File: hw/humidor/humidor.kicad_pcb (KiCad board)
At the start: 2 copper layers, 79 x 53 mm, 26 parts, among them J1 PWR IN, J2 PWR IN/EXTSENS/IND, J3 IN_SENSOR, J4 Conn_01x05, J5 HEAT/FAN/HS, Q1 2N7002, Q2 IRFD9120, Q3 IRL540, SW1 SW_Push, U1 LT1086-ADJ

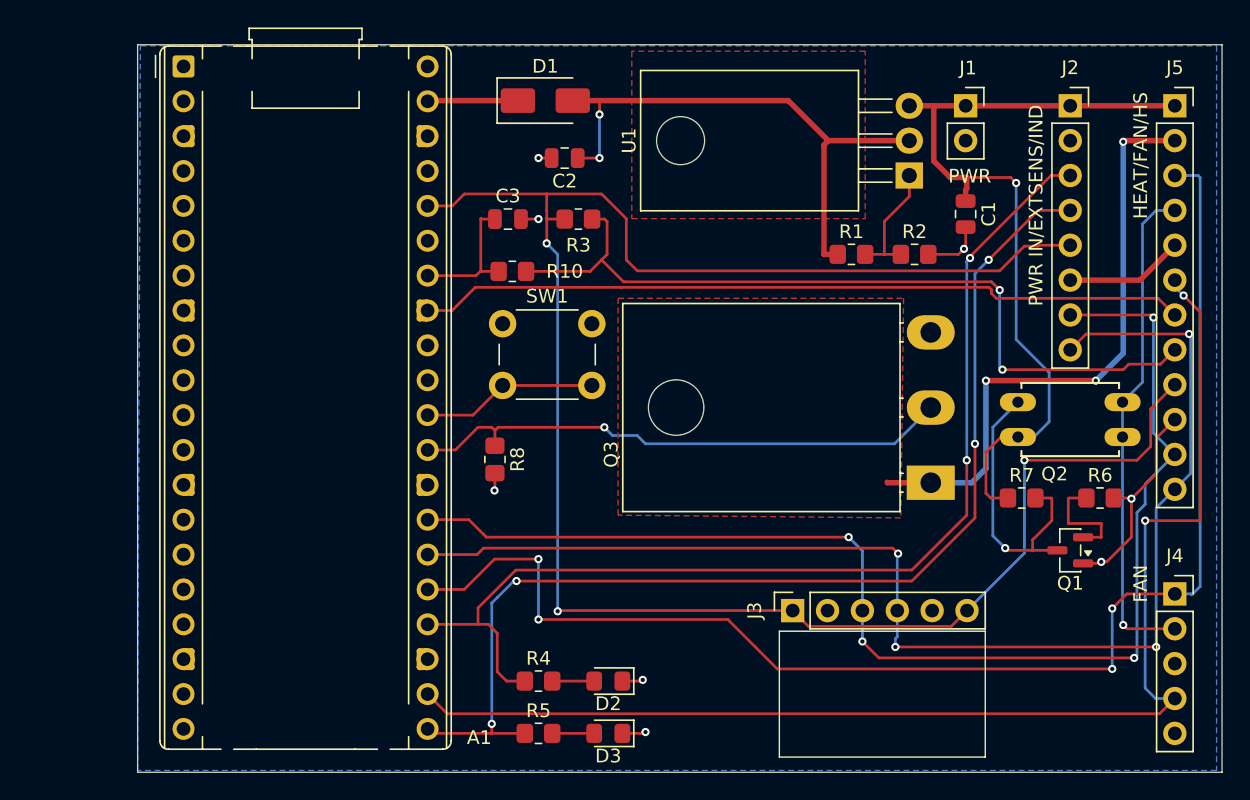
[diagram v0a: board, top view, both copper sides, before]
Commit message: finalized board with all DRC satisfied. Next step is to try double side layout.
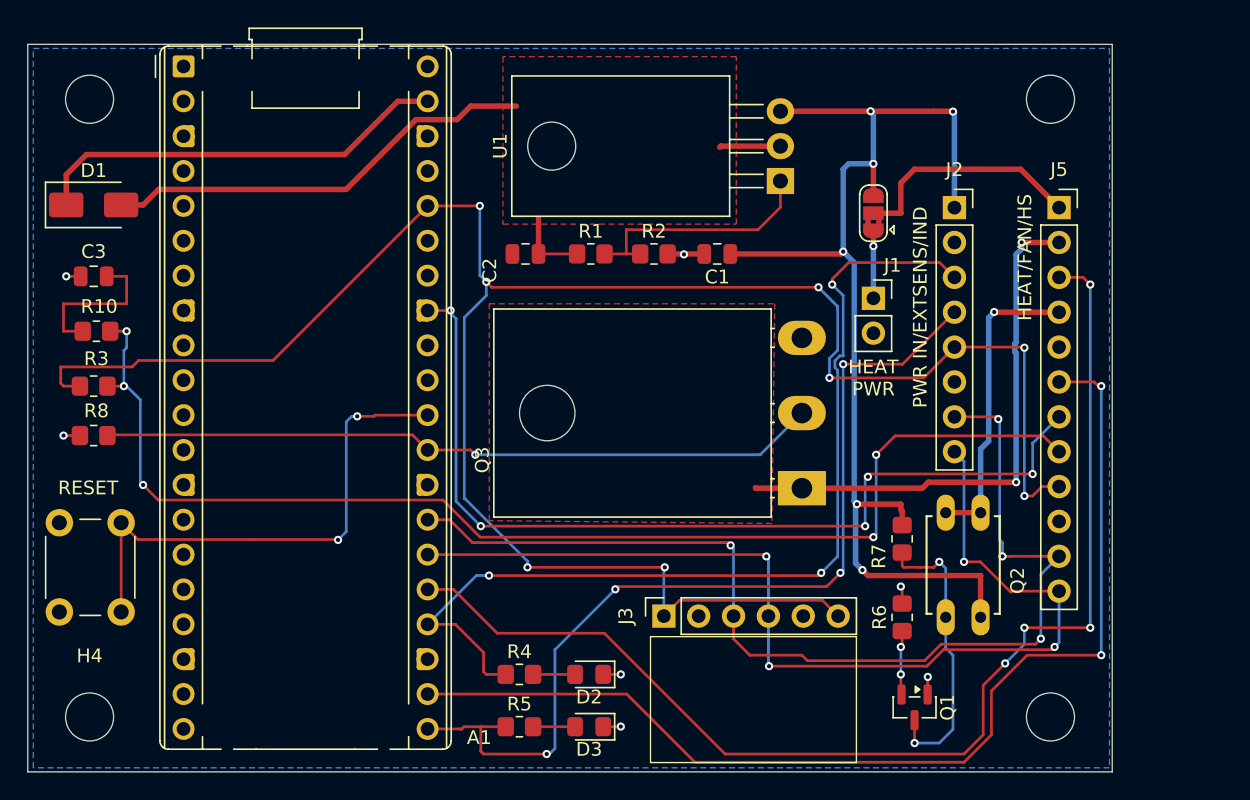
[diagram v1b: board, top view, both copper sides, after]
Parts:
- removed J4: Conn_01x05, Connector_PinSocket_2.54mm:PinSocket_1x05_P2.54mm_Vertical
- added H1: MountingHole, MountingHole:MountingHole_3.5mm, F.Cu at (153.5, 53.5)
- added H2: MountingHole, MountingHole:MountingHole_3.5mm, F.Cu at (153.5, 98.5)
- added H3: MountingHole, MountingHole:MountingHole_3.5mm, F.Cu at (83.5, 53.5)
- added H4: MountingHole, MountingHole:MountingHole_3.5mm, F.Cu at (83.5, 98.5)
- added JP2: SolderJumper_3_Bridged12, Jumper:SolderJumper-3_P1.3mm_Bridged2Bar12_RoundedPad1.0x1.5mm, F.Cu at (140.6, 61.8)
- moved SW1 38.5 mm to (81.3, 90.8), turned to 90 degrees
- moved R3 37.3 mm to (83.8, 74.4)
- moved D1 33.8 mm to (83.8, 61.2)
- moved R10 30.6 mm to (84.0, 70.4)
- moved C3 30.5 mm to (83.8, 66.4), turned to 180 degrees
- moved R8 29.3 mm to (83.8, 78.0), turned to 180 degrees
- moved R1 19.0 mm to (120.0, 64.8)
- moved R2 19.0 mm to (124.6, 64.8)
- moved C1 18.3 mm to (129.2, 64.8), turned to 180 degrees
- moved R6 16.8 mm to (142.7, 91.2), turned to 90 degrees
- moved Q1 16.1 mm to (143.6, 97.8), turned to -90 degrees
- moved J1 15.6 mm to (140.6, 68.0)
- moved Q2 13.2 mm to (147.1, 87.4), turned to -90 degrees
- moved J2 11.2 mm to (146.5, 61.4)
- moved J5 11.2 mm to (154.1, 61.4)
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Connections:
- J1 pad 1: +12V -> Net-(J1-Pin_1)
- J5 pad 1: +12V -> /HEAT_PWR
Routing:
- net /T_HEATSINK: track 58.9 -> 89.6 mm, vias 2 -> 5
- net GND: track 35.3 -> 10.1 mm, vias 8 -> 7
- net Net-(A1-RUN): track 12.9 -> 37.8 mm, vias 0 -> 2
- net Net-(A1-VSYS): track 6.60 -> 30.7 mm
- net +12V: track 60.4 -> 82.9 mm, vias 1 -> 6
- net /SDA0: track 93.5 -> 74.6 mm
- net /HEAT_PWR: track 0.00 -> 17.3 mm
- net /SCL0: track 92.3 -> 77.5 mm
- net /FAN_PWR: track 36.5 -> 22.3 mm
- net /FAN_PWM: track 92.5 -> 79.0 mm
- net /FAN_ON: track 81.1 -> 68.5 mm
- net +3.3V: track 142.4 -> 155.0 mm, vias 3 -> 8
- net /TACH: track 99.9 -> 87.4 mm
- net /HEAT_PWM: track 40.2 -> 52.5 mm
- net /AGND: track 56.1 -> 67.0 mm, vias 0 -> 5
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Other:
- board text added: "HEAT PWR"
- board text added: "RESET"
- board text removed: "FAN"
- board text removed: "PWR"
